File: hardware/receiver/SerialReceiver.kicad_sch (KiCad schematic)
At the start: 30 parts, among them J1 DATA, J2 CONTROL, J3 RX, J4 Clock select, J5 Conn_01x03_Male, J6 Clock select, SW1 SW_Push, U1 74HC132, U2 74HC191, U3 74HC191, U4 74HC595, U5 74HC74, U6 74LS244

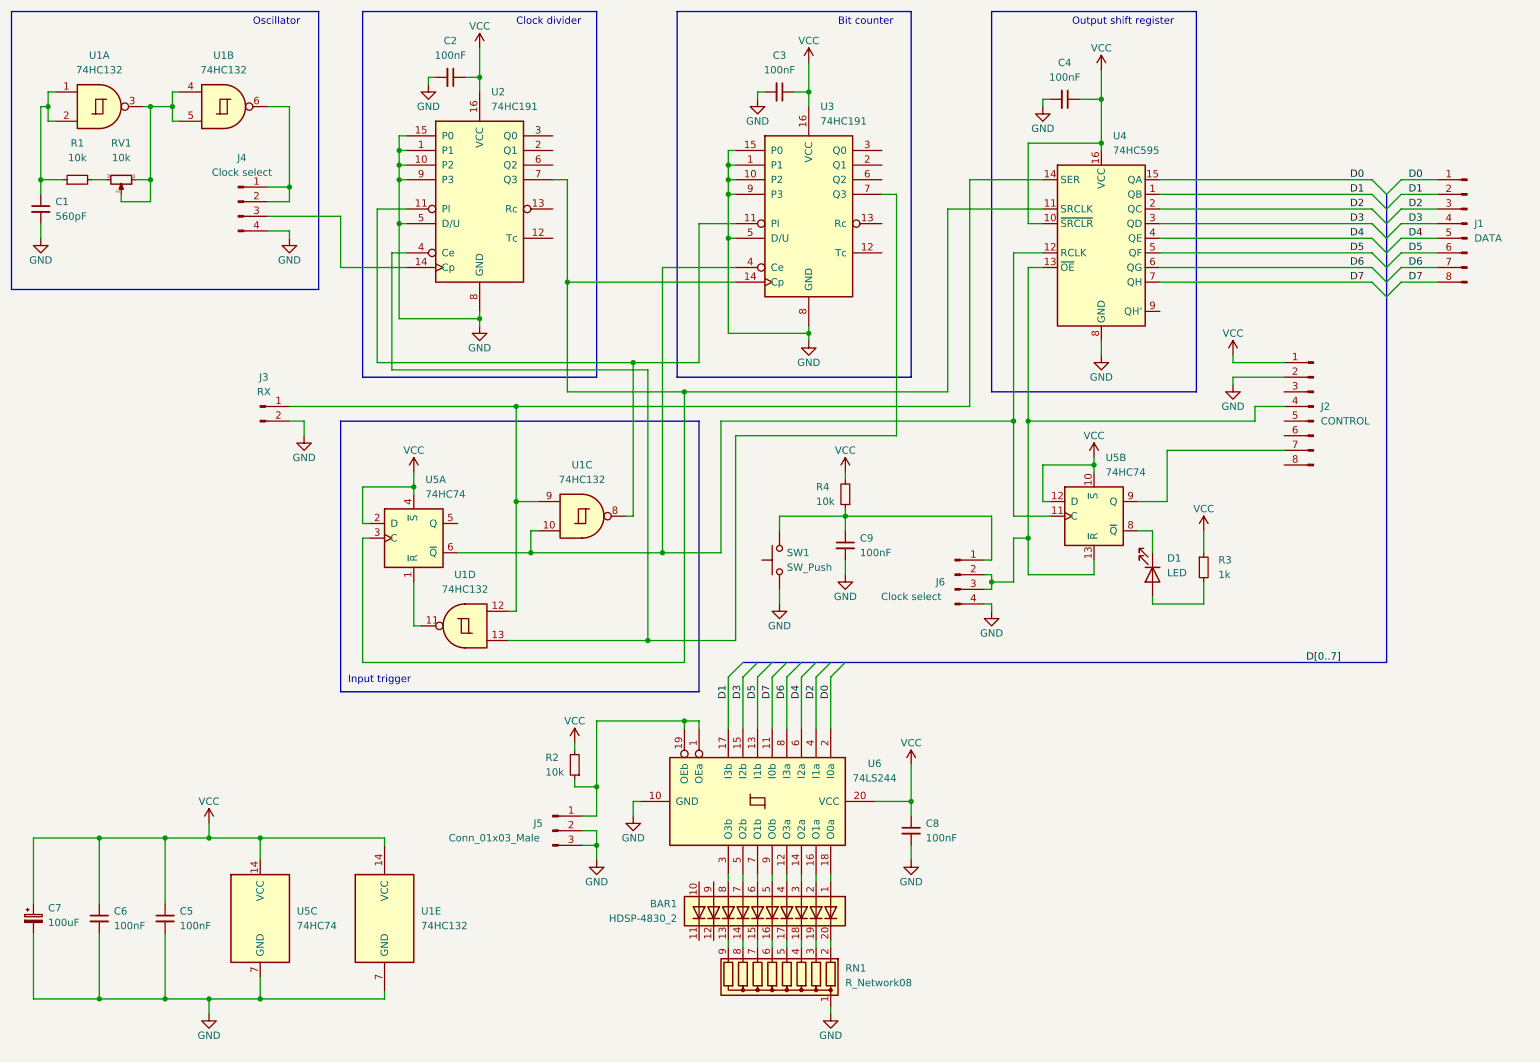
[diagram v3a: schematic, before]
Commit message: Changed the layout of the schematic for better wiring.
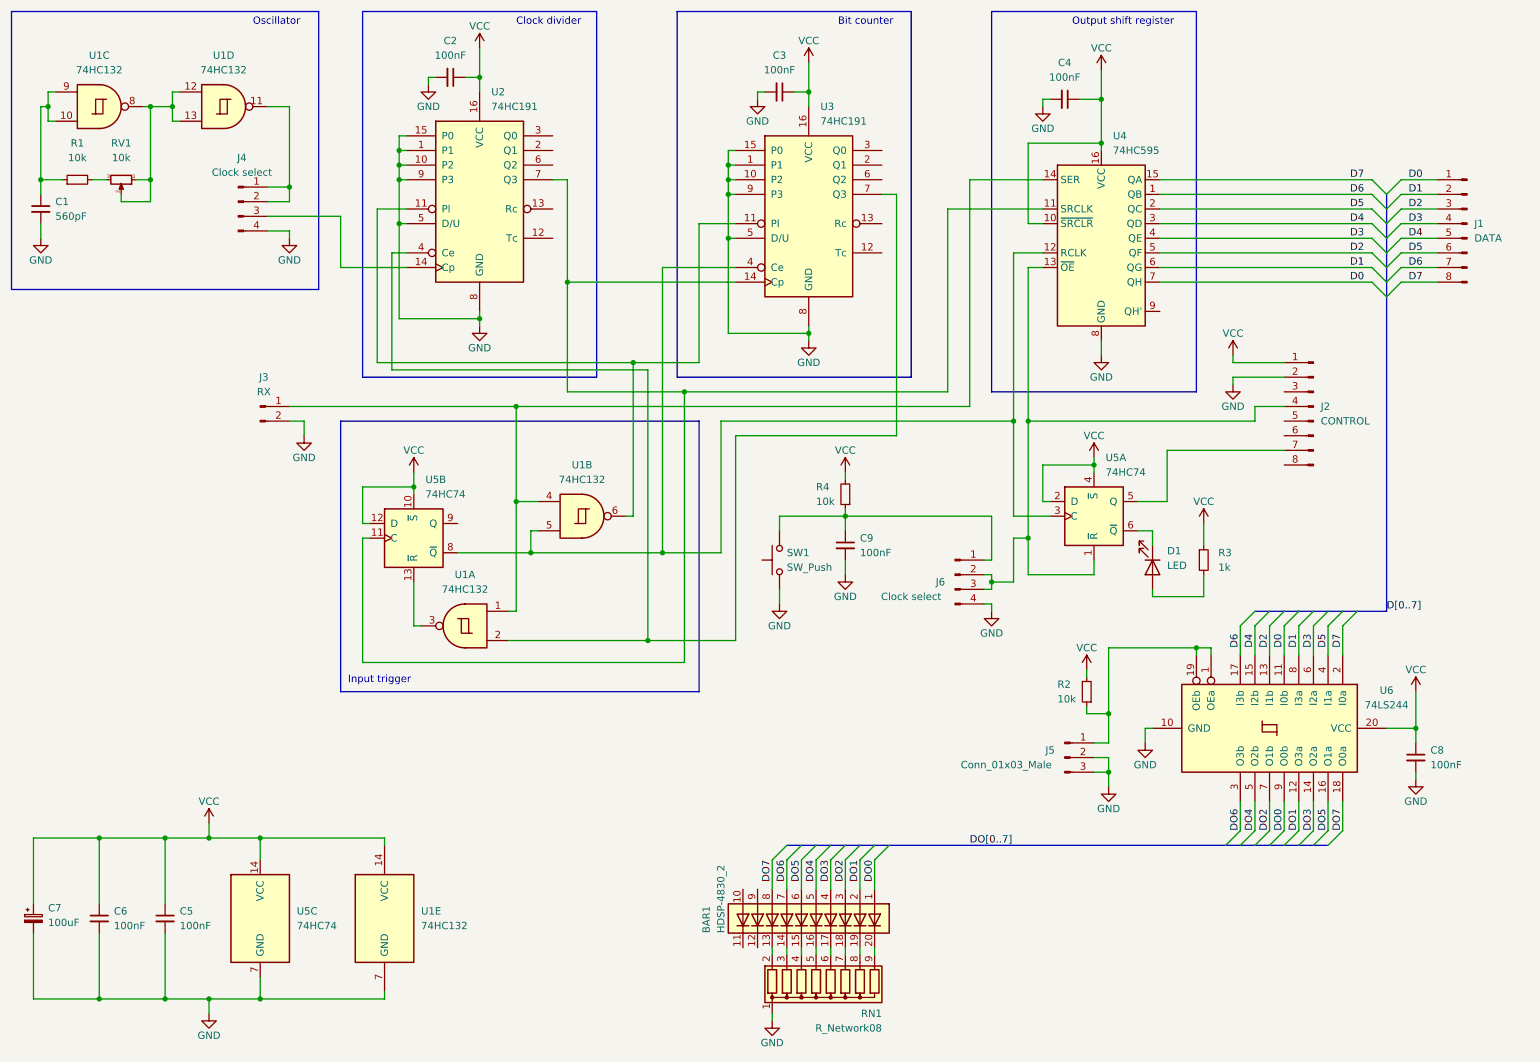
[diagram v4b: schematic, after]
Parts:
- BAR1: footprint Display:HDSP-4830 -> Package_DIP:DIP-20_W7.62mm_Socket
- RV1: footprint Resistor_THT:R_Axial_DIN0207_L6.3mm_D2.5mm_P10.16mm_Horizontal -> Potentiometer_THT:Potentiometer_Bourns_3296W_Vertical
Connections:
- net D0: now also U4.7 (QH), U6.11 (I0b); no longer U4.15 (QA), U6.2 (I0a)
- net D1: now also U4.6 (QG), U6.8 (I3a); no longer U4.1 (QB), U6.17 (I3b)
- net D2: now also U4.5 (QF), U6.13 (I1b); no longer U4.2 (QC), U6.4 (I1a)
- net D3: now also U4.4 (QE), U6.6 (I2a); no longer U4.3 (QD), U6.15 (I2b)
- net D4: now also U4.3 (QD), U6.15 (I2b); no longer U4.4 (QE), U6.6 (I2a)
- net D5: now also U4.2 (QC), U6.4 (I1a); no longer U4.5 (QF), U6.13 (I1b)
- net D6: now also U4.1 (QB), U6.17 (I3b); no longer U4.6 (QG), U6.8 (I3a)
- net D7: now also U4.15 (QA), U6.2 (I0a); no longer U4.7 (QH), U6.11 (I0b)
- net at C1.1, R1.1: now also U1.10, U1.9; no longer U1.1, U1.2
- net DO0: now reaches BAR1.1 (A)
- net DO0: now also U6.9 (O0b); no longer U6.18 (O0a)
- net at BAR1.13 (K): now also RN1.2 (R1); no longer RN1.9 (R8)
- net at BAR1.14 (K): now also RN1.3 (R2); no longer RN1.8 (R7)
- net at BAR1.15 (K): now also RN1.4 (R3); no longer RN1.7 (R6)
- net at BAR1.16 (K): now also RN1.5 (R4); no longer RN1.6 (R5)
- net at BAR1.17 (K): now also RN1.6 (R5); no longer RN1.5 (R4)
- net at BAR1.18 (K): now also RN1.7 (R6); no longer RN1.4 (R3)
- net at BAR1.19 (K): now also RN1.8 (R7); no longer RN1.3 (R2)
- net DO1: now reaches BAR1.2 (A)
- net DO1: now also U6.12 (O3a); no longer U6.16 (O1a)
- net at BAR1.20 (K): now also RN1.9 (R8); no longer RN1.2 (R1)
- net DO2: now reaches BAR1.3 (A)
- net DO2: now also U6.7 (O1b); no longer U6.14 (O2a)
- net DO3: now reaches BAR1.4 (A)
- net DO3: now also U6.14 (O2a); no longer U6.12 (O3a)
- net DO4: now reaches BAR1.5 (A)
- net DO4: now also U6.5 (O2b); no longer U6.9 (O0b)
- net DO5: now reaches BAR1.6 (A)
- net DO5: now also U6.16 (O1a); no longer U6.7 (O1b)
- net DO6: now reaches BAR1.7 (A)
- net DO6: now also U6.3 (O3b); no longer U6.5 (O2b)
- net DO7: now reaches BAR1.8 (A)
- net DO7: now also U6.18 (O0a); no longer U6.3 (O3b)
- net at J4.1 (Pin_1), J4.2 (Pin_2): now also U1.11; no longer U1.6
- net at J3.1 (Pin_1), U4.14 (SER): now also U1.1, U1.4; no longer U1.12, U1.9
- net at U2.11 (Pl), U3.11 (Pl): now also U1.6; no longer U1.8
- net at U2.4 (Ce), U3.7 (Q3): now also U1.2; no longer U1.13
- net at U2.7 (Q3), U3.14 (Cp), U4.11 (SRCLK): now also U5.11 (C); no longer U5.3 (C)
- net at J2.4 (Pin_4), J6.2 (Pin_2), J6.3 (Pin_3)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: now also U5.1 (~{R}); no longer U5.13 (~{R})
- net at U5.8 (~{Q}): now also U1.5, U3.4 (Ce), U4.12 (RCLK), U5.3 (C); no longer D1.1 (K)
- net at U5.9 (Q): no longer J2.7 (Pin_7)
- net at U5.5 (Q): now also J2.7 (Pin_7)
- new net: U1.3, U5.13 (~{R})
- new net: D1.1 (K), U5.6 (~{Q})
- new net: RV1.1, RV1.2, U1.12, U1.13, U1.8
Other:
- moved on the sheet: BAR1, C8, D1, J5, R2, R3, RN1, U1A, U1B, U1C, U1D, U5A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

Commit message: Made an RX input protection, and almost finished the PCB.
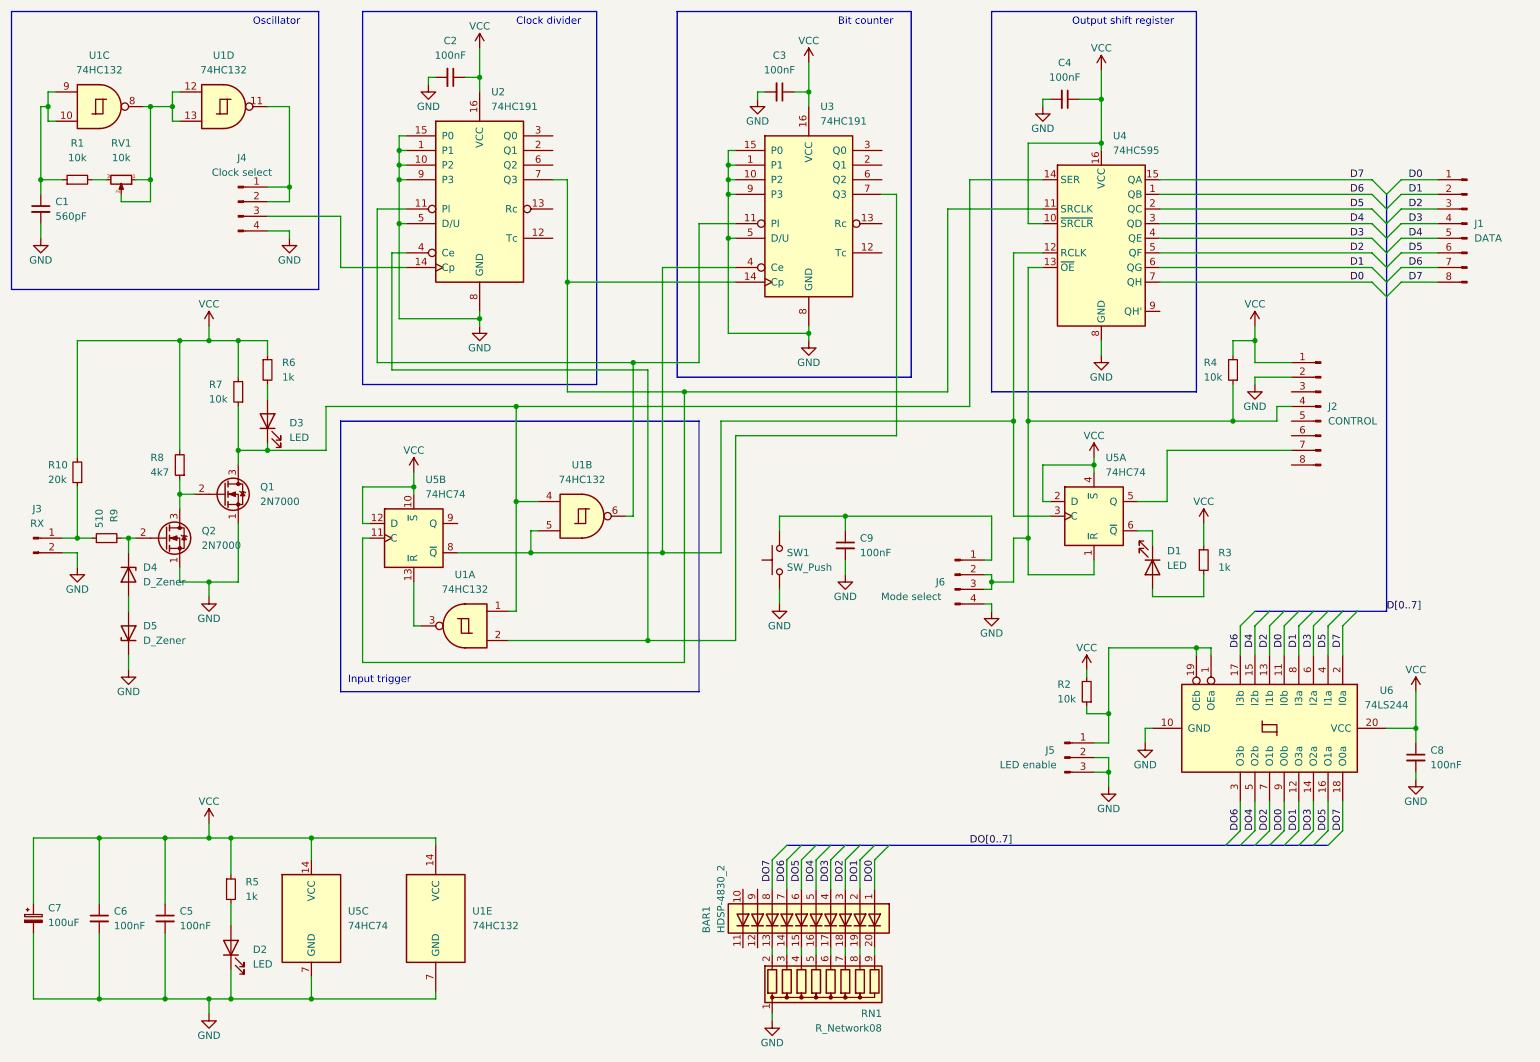
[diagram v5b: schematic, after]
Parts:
- added D2, D3: LED, LED_THT:LED_D3.0mm, symbol Device:LED
- added D4, D5: D_Zener, symbol Device:D_Zener
- added Q1, Q2: 2N7000, Package_TO_SOT_THT:TO-92_Inline, symbol Transistor_FET:2N7000
- added R10: 20k, Resistor_THT:R_Axial_DIN0207_L6.3mm_D2.5mm_P10.16mm_Horizontal, symbol Device:R_Small
- added R5, R6: 1k, Resistor_THT:R_Axial_DIN0207_L6.3mm_D2.5mm_P10.16mm_Horizontal, symbol Device:R_Small
- added R7: 10k, Resistor_THT:R_Axial_DIN0207_L6.3mm_D2.5mm_P10.16mm_Horizontal, symbol Device:R_Small
- added R8: 4k7, Resistor_THT:R_Axial_DIN0207_L6.3mm_D2.5mm_P10.16mm_Horizontal, symbol Device:R_Small
- added R9: 510, Resistor_THT:R_Axial_DIN0207_L6.3mm_D2.5mm_P10.16mm_Horizontal, symbol Device:R_Small
- J5: value Conn_01x03_Male -> LED enable
- J6: value Clock select -> Mode select
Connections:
- net GND: now also D2.1 (K), D5.1 (K), Q1.1 (S), Q2.1 (S)
- net VCC: now also R10.2, R5.1, R6.1, R7.2, R8.2
- net at C9.1, J6.1 (Pin_1), SW1.2: no longer R4.1
- net at U1.1, U1.4, U4.14 (SER): now also D3.1 (K), Q1.3 (D), R7.1; no longer J3.1 (Pin_1)
- net at J2.4 (Pin_4), J6.2 (Pin_2), J6.3 (Pin_3)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: now also R4.1
- new net: J3.1 (Pin_1), R10.1, R9.1
- new net: D3.2 (A), R6.2
- new net: D2.2 (A), R5.2
- new net: D4.1 (K), Q2.2 (G), R9.2
- new net: Q1.2 (G), Q2.3 (D), R8.1
- new net: D4.2 (A), D5.2 (A)
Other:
- moved on the sheet: J2, J3, R4, U1E, U5C

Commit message: Input protection is now on the PCB.
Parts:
- D4, D5: footprint (none) -> Diode_THT:D_DO-35_SOD27_P7.62mm_Horizontal
- Q1, Q2: footprint Package_TO_SOT_THT:TO-92_Inline -> Package_TO_SOT_THT:TO-92_Inline_Wide
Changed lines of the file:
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@@
   (symbol (lib_id "power:GND") (at 35.56 129.54 0) (unit 1)
     (in_bom yes) (on_board yes)
-    (property "Reference" "#PWR?" (id 0) (at 35.56 135.89 0)
+    (property "Reference" "#PWR0130" (id 0) (at 35.56 135.89 0)
       (effects (font (size 1.27 1.27)) hide)
     )
@@
   (symbol (lib_id "power:GND") (at 49.53 116.84 0) (unit 1)
     (in_bom yes) (on_board yes)
-    (property "Reference" "#PWR?" (id 0) (at 49.53 123.19 0)
+    (property "Reference" "#PWR0104" (id 0) (at 49.53 123.19 0)
       (effects (font (size 1.27 1.27)) hide)
     )
@@
   (symbol (lib_id "power:GND") (at 26.67 111.76 0) (unit 1)
     (in_bom yes) (on_board yes)
-    (property "Reference" "#PWR?" (id 0) (at 26.67 118.11 0)
+    (property "Reference" "#PWR0129" (id 0) (at 26.67 118.11 0)
       (effects (font (size 1.27 1.27)) hide)
     )
@@
       (effects (font (size 1.27 1.27)) (justify left))
     )
-    (property "Footprint" "Package_TO_SOT_THT:TO-92_Inline" (id 2) (at 46.99 108.585 0)
+    (property "Footprint" "Package_TO_SOT_THT:TO-92_Inline_Wide" (id 2) (at 46.99 108.585 0)
       (effects (font (size 1.27 1.27) italic) (justify left) hide)
     )
@@
       (effects (font (size 1.27 1.27)) (justify left))
     )
-    (property "Footprint" "Package_TO_SOT_THT:TO-92_Inline" (id 2) (at 57.15 100.965 0)
+    (property "Footprint" "Package_TO_SOT_THT:TO-92_Inline_Wide" (id 2) (at 57.15 100.965 0)
       (effects (font (size 1.27 1.27) italic) (justify left) hide)
     )
@@
       (effects (font (size 1.27 1.27)) (justify right))
     )
-    (property "Footprint" "" (id 2) (at 35.56 123.19 0)
+    (property "Footprint" "Diode_THT:D_DO-35_SOD27_P7.62mm_Horizontal" (id 2) (at 35.56 123.19 0)
       (effects (font (size 1.27 1.27)) hide)
     )
@@
       (effects (font (size 1.27 1.27)) (justify left))
     )
-    (property "Footprint" "" (id 2) (at 35.56 113.03 0)
+    (property "Footprint" "Diode_THT:D_DO-35_SOD27_P7.62mm_Horizontal" (id 2) (at 35.56 113.03 0)
       (effects (font (size 1.27 1.27)) hide)
     )
@@
   (symbol (lib_id "power:VCC") (at 49.53 69.85 0) (unit 1)
     (in_bom yes) (on_board yes)
-    (property "Reference" "#PWR?" (id 0) (at 49.53 73.66 0)
+    (property "Reference" "#PWR0131" (id 0) (at 49.53 73.66 0)
       (effects (font (size 1.27 1.27)) hide)
     )
@@
       (reference "#PWR0103") (unit 1) (value "VCC") (footprint "")
     )
+    (path "/417f674b-bdb9-48ef-b416-ca138410890e"
+      (reference "#PWR0104") (unit 1) (value "GND") (footprint "")
+    )
     (path "/0386306f-2d64-4988-a980-0991b97b2de6"
       (reference "#PWR0105") (unit 1) (value "VCC") (footprint "")
@@
       (reference "#PWR0128") (unit 1) (value "GND") (footprint "")
     )
+    (path "/8c5e2675-d70d-40de-85e0-5f9eac4a8add"
+      (reference "#PWR0129") (unit 1) (value "GND") (footprint "")
+    )
     (path "/367df4f2-41a7-4b15-83e4-8e53f2d8c90b"
-      (reference "#PWR?") (unit 1) (value "GND") (footprint "")
-    )
-    (path "/417f674b-bdb9-48ef-b416-ca138410890e"
-      (reference "#PWR?") (unit 1) (value "GND") (footprint "")
-    )
-    (path "/8c5e2675-d70d-40de-85e0-5f9eac4a8add"
-      (reference "#PWR?") (unit 1) (value "GND") (footprint "")
+      (reference "#PWR0130") (unit 1) (value "GND") (footprint "")
     )
     (path "/fbbd389c-4d23-48f5-8d19-599201ce1aa0"
-      (reference "#PWR?") (unit 1) (value "VCC") (footprint "")
+      (reference "#PWR0131") (unit 1) (value "VCC") (footprint "")
     )
     (path "/32a5359d-11b0-4135-8a7a-97e9e04588a6"
@@
     )
     (path "/f9933f78-91da-4899-a4d9-92550d833586"
-      (reference "D4") (unit 1) (value "D_Zener") (footprint "")
+      (reference "D4") (unit 1) (value "D_Zener") (footprint "Diode_THT:D_DO-35_SOD27_P7.62mm_Horizontal")
     )
     (path "/f02abf00-893e-418f-b7a3-be9998d75d19"
-      (reference "D5") (unit 1) (value "D_Zener") (footprint "")
+      (reference "D5") (unit 1) (value "D_Zener") (footprint "Diode_THT:D_DO-35_SOD27_P7.62mm_Horizontal")
     )
     (path "/64b60641-454f-40ba-aa1b-62f2332f3498"
@@
     )
     (path "/be0da254-51f4-4c04-b4b2-44b490bfbb02"
-      (reference "Q1") (unit 1) (value "2N7000") (footprint "Package_TO_SOT_THT:TO-92_Inline")
+      (reference "Q1") (unit 1) (value "2N7000") (footprint "Package_TO_SOT_THT:TO-92_Inline_Wide")
     )
     (path "/92284ce1-25bd-4332-b5ed-123c58b4cd54"
-      (reference "Q2") (unit 1) (value "2N7000") (footprint "Package_TO_SOT_THT:TO-92_Inline")
+      (reference "Q2") (unit 1) (value "2N7000") (footprint "Package_TO_SOT_THT:TO-92_Inline_Wide")
     )
     (path "/646a899c-2205-474b-8b4e-750a9d6479fc"
